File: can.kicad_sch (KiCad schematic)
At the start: 17 parts, among them J17 BM04B-GHS-TBT(LF)(SN)(N), U17 TJA1042TK-3

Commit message: da
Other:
- company: (none) -> TampanTech
- title: (none) -> Can
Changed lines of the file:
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@@
 	(generator_version "8.0")
 	(paper "A4")
+	(title_block
+		(title "Can")
+		(date "2024-09-08")
+		(rev "1")
+		(company "TampanTech")
+		(comment 1 "Drone Flight Management Unit")
+	)
 	(junction
 		(at 128.27 64.77)

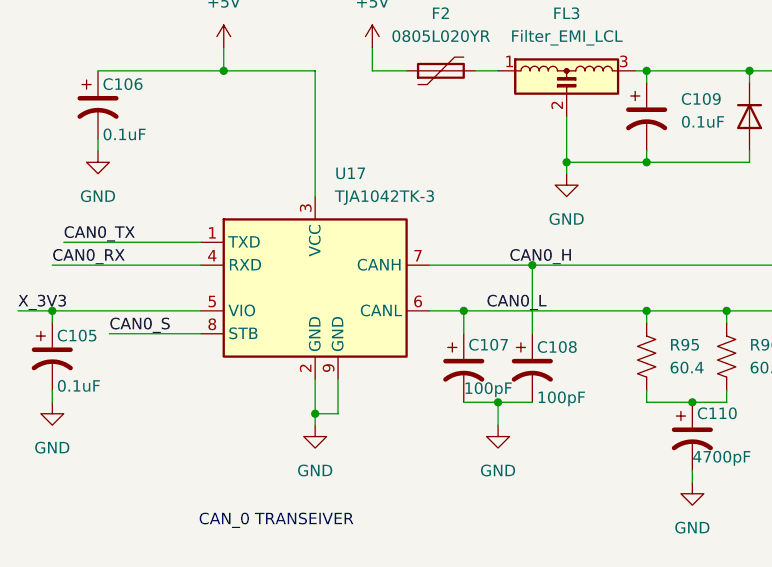
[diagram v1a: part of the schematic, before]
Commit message: change label to global
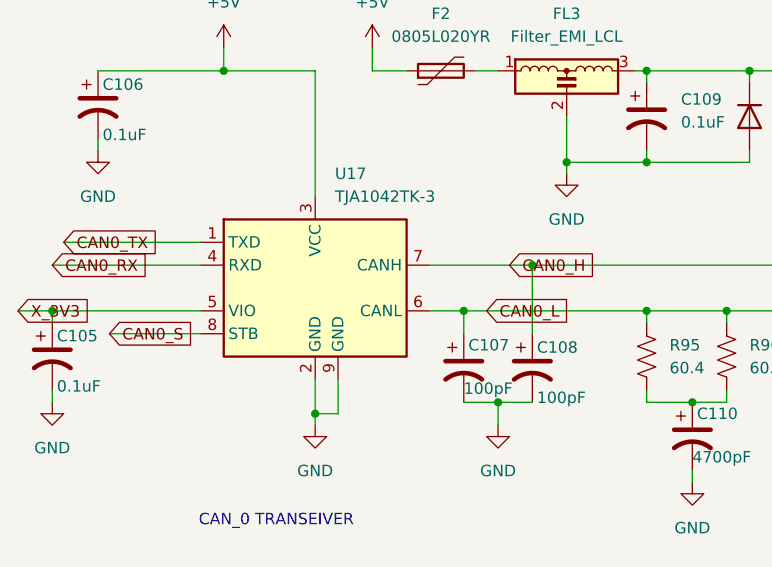
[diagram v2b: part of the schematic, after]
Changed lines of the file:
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@@
 		)
 	)
-	(label "CAN0_H"
+	(global_label "CAN0_L"
+		(shape input)
+		(at 119.38 81.28 0)
+		(fields_autoplaced yes)
+		(effects
+			(font
+				(size 1.27 1.27)
+			)
+			(justify left)
+		)
+		(property "Intersheetrefs" "${INTERSHEET_REFS}"
+			(at 129.2595 81.28 0)
+			(effects
+				(font
+					(size 1.27 1.27)
+				)
+				(justify left)
+				(hide yes)
+			)
+		)
+	)
+	(global_label "CAN0_H"
+		(shape input)
 		(at 121.92 76.2 0)
 		(fields_autoplaced yes)
@@
 				(size 1.27 1.27)
 			)
-			(justify left bottom)
+			(justify left)
+		)
+		(property "Intersheetrefs" "${INTERSHEET_REFS}"
+			(at 132.1019 76.2 0)
+			(effects
+				(font
+					(size 1.27 1.27)
+				)
+				(justify left)
+				(hide yes)
+			)
 		)
 	)
-	(label "CAN0_TX"
+	(global_label "CAN0_RX"
+		(shape input)
+		(at 71.12 76.2 0)
+		(fields_autoplaced yes)
+		(effects
+			(font
+				(size 1.27 1.27)
+			)
+			(justify left)
+		)
+		(property "Intersheetrefs" "${INTERSHEET_REFS}"
+			(at 82.4509 76.2 0)
+			(effects
+				(font
+					(size 1.27 1.27)
+				)
+				(justify left)
+				(hide yes)
+			)
+		)
+	)
+	(global_label "CAN0_S"
+		(shape input)
+		(at 77.47 83.82 0)
+		(fields_autoplaced yes)
+		(effects
+			(font
+				(size 1.27 1.27)
+			)
+			(justify left)
+		)
+		(property "Intersheetrefs" "${INTERSHEET_REFS}"
+			(at 87.5309 83.82 0)
+			(effects
+				(font
+					(size 1.27 1.27)
+				)
+				(justify left)
+				(hide yes)
+			)
+		)
+	)
+	(global_label "X_3V3"
+		(shape input)
+		(at 67.31 81.28 0)
+		(fields_autoplaced yes)
+		(effects
+			(font
+				(size 1.27 1.27)
+			)
+			(justify left)
+		)
+		(property "Intersheetrefs" "${INTERSHEET_REFS}"
+			(at 75.9799 81.28 0)
+			(effects
+				(font
+					(size 1.27 1.27)
+				)
+				(justify left)
+				(hide yes)
+			)
+		)
+	)
+	(global_label "CAN0_TX"
+		(shape input)
 		(at 72.39 73.66 0)
 		(fields_autoplaced yes)
@@
 				(size 1.27 1.27)
 			)
-			(justify left bottom)
+			(justify left)
+		)
+		(property "Intersheetrefs" "${INTERSHEET_REFS}"
+			(at 83.4185 73.66 0)
+			(effects
+				(font
+					(size 1.27 1.27)
+				)
+				(justify left)
+				(hide yes)
+			)
 		)
 	)
-	(label "CAN0_RX"
-		(at 71.12 76.2 0)
-		(fields_autoplaced yes)
-		(effects
-			(font
-				(size 1.27 1.27)
-			)
-			(justify left bottom)
-		)
-	)
-	(label "CAN0_L"
-		(at 119.38 81.28 0)
-		(fields_autoplaced yes)
-		(effects
-			(font
-				(size 1.27 1.27)
-			)
-			(justify left bottom)
-		)
-	)
-	(label "X_3V3"
-		(at 67.31 81.28 0)
-		(fields_autoplaced yes)
-		(effects
-			(font
-				(size 1.27 1.27)
-			)
-			(justify left bottom)
-		)
-	)
-	(label "CAN0_S"
-		(at 77.47 83.82 0)
-		(fields_autoplaced yes)
-		(effects
-			(font
-				(size 1.27 1.27)
-			)
-			(justify left bottom)
-		)
-	)
